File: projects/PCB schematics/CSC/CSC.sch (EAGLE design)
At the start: 23 parts, among them Q1 IRLZ44Z, Q2 IRLZ44Z

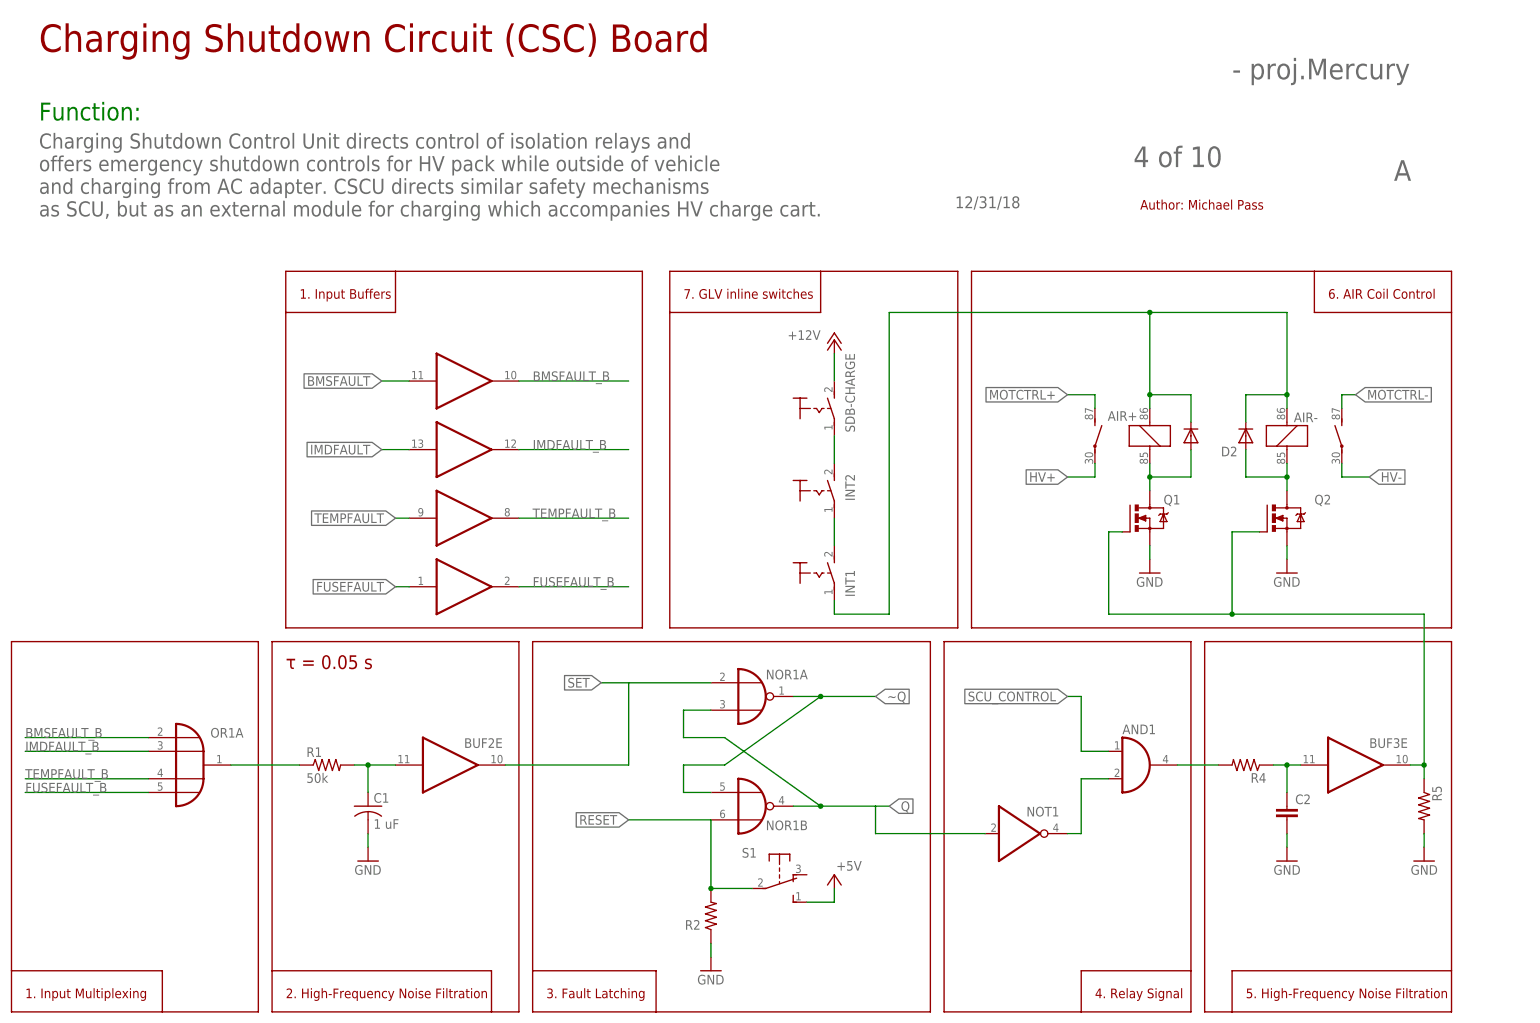
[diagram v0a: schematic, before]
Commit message: SC - Rev A; First PCB revision complete.
This marks the first draft of the SC board.
Parts have been laid out and initial routing completed through
extensive use of autorouter.
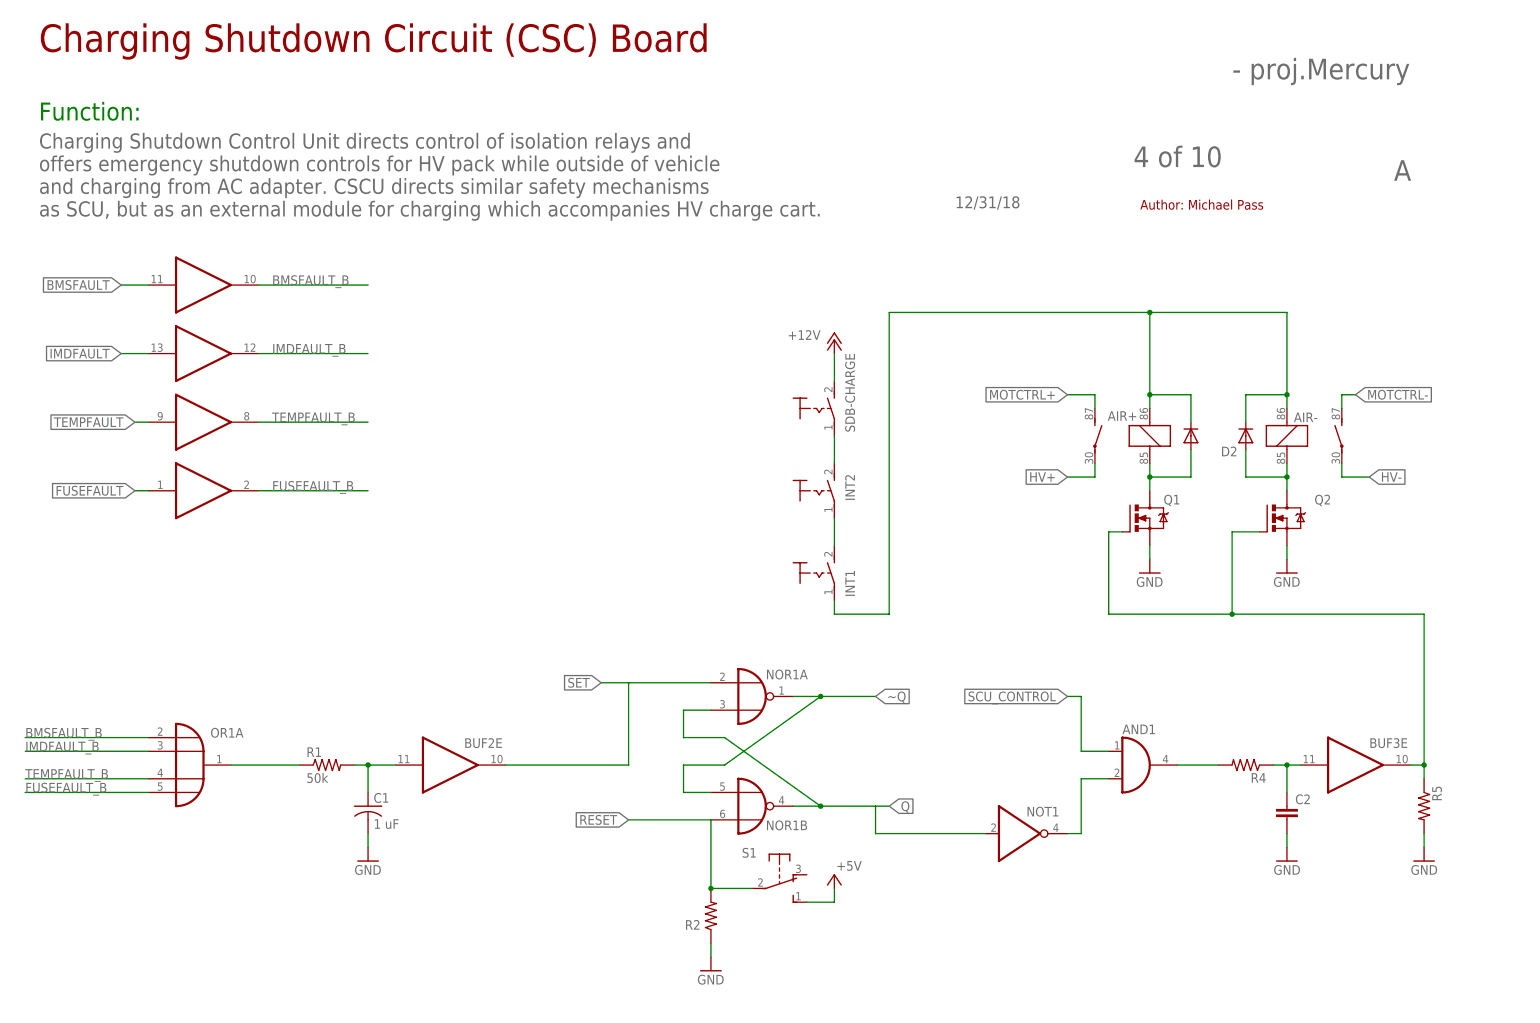
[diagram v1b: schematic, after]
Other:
- note removed: "1. Input Buffers"
- note removed: "1. Input Multiplexing"
- note removed: "2. High-Frequency Noise Filtration"
- note removed: "3. Fault Latching"
- note removed: "4. Relay Signal"
- note removed: "5. High-Frequency Noise Filtration"
- note removed: "6. AIR Coil Control"
- note removed: "7. GLV inline switches"
- note removed: "τ = 0.05 s"
